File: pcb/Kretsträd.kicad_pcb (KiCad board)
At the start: 2 copper layers, 112.5 x 95.1 mm, 58 parts, among them J1 Conn_01x02_Female, J2 Conn_01x02_Female, J3 Conn_01x02_Female, SW1 SW_PUSH, SW10 SW_PUSH, SW11 SW_PUSH, SW12 SW_PUSH, SW13 SW_PUSH, SW14 SW_PUSH, SW15 SW_PUSH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

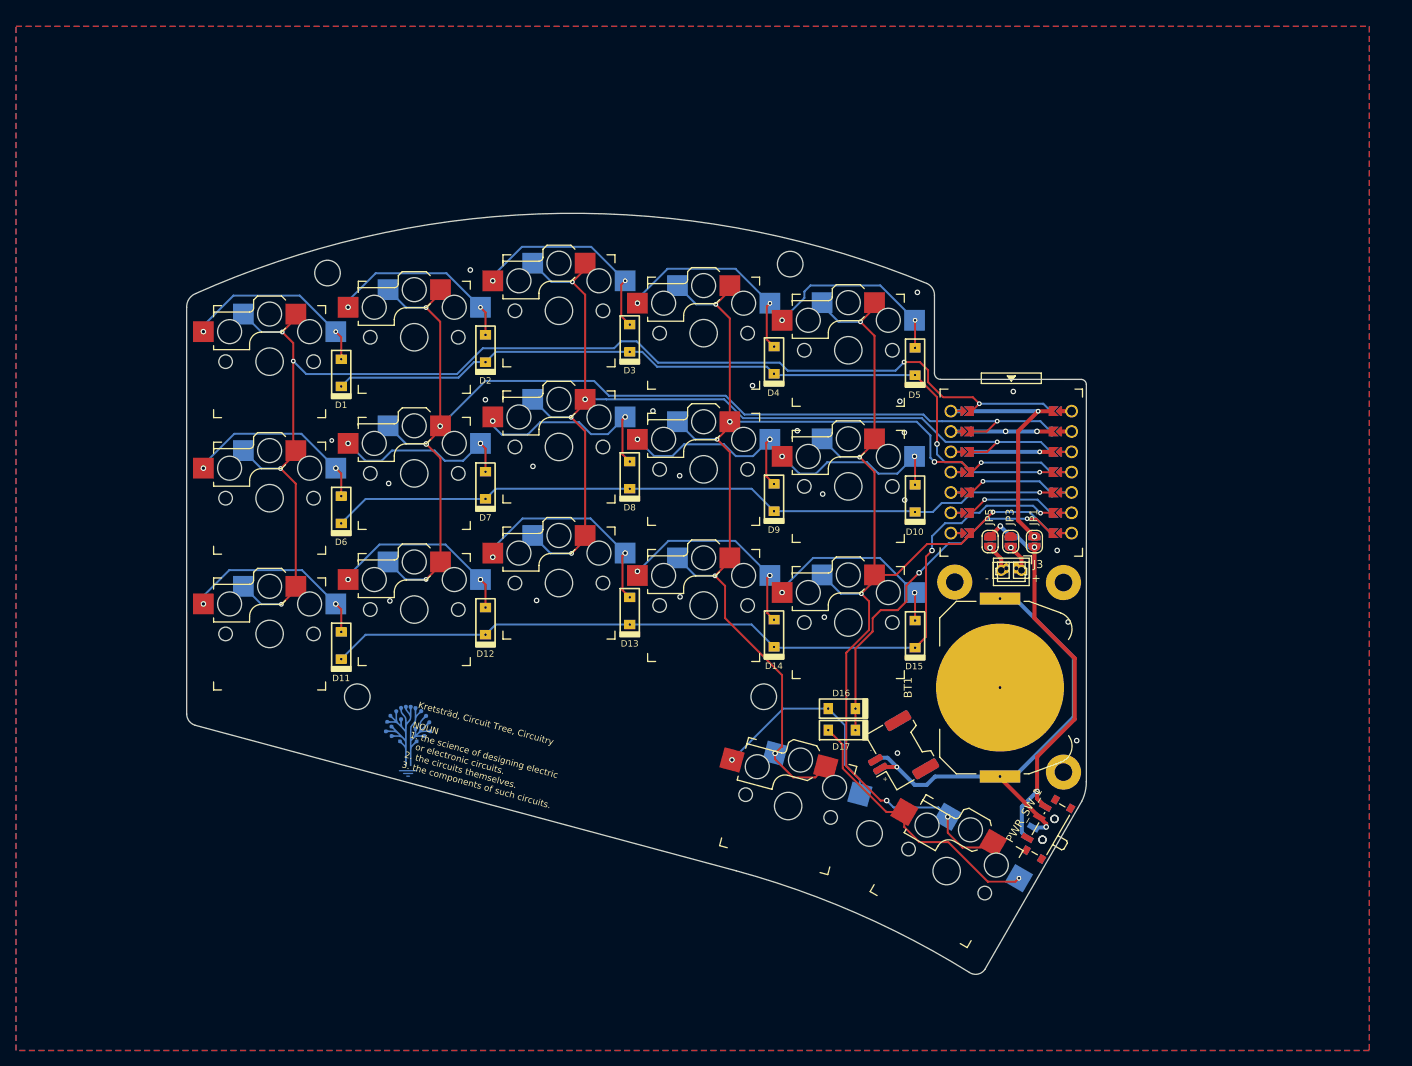
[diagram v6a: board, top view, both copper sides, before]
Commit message: 1. Updated switch footprint to increase solder pad size. 2. Squeezed MCU LIR2032 battery holder power switch section. 3. Re-routed a lot. 4. Reduced curvature on edge under thumb keys. 5. Removed power and ground pins selector jumper pads beneath MCU. 6. Other changes.
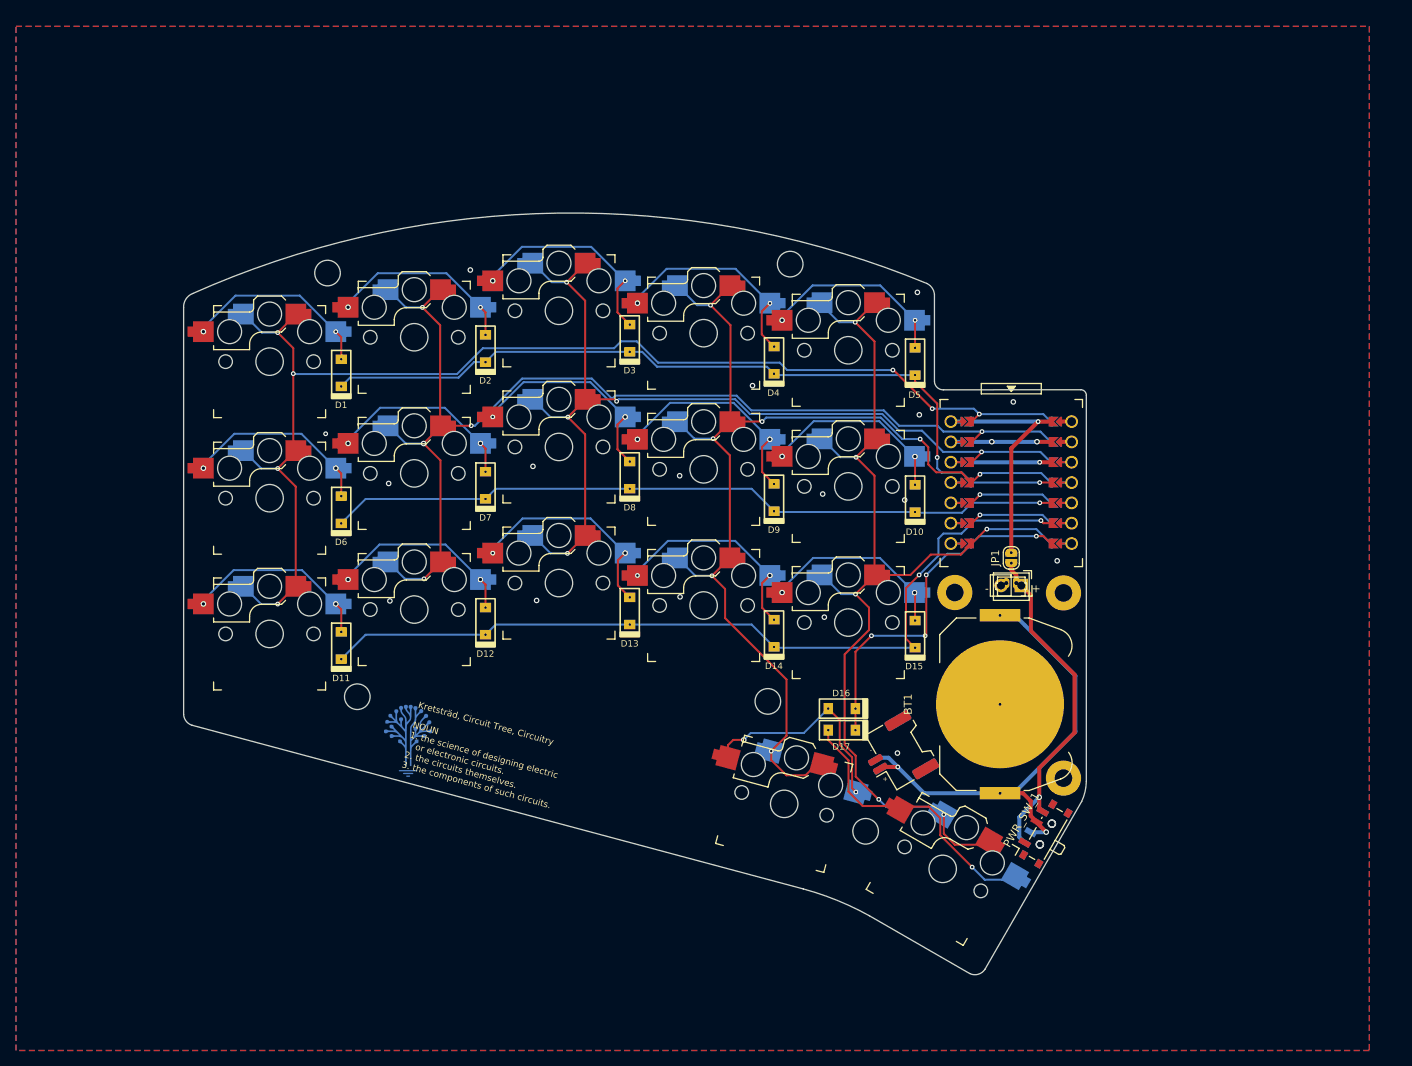
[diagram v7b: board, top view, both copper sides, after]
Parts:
- removed Hole_1, Hole_2: MountingHole_Pad, kbd:1pin_conn
- removed JP2: to_RAW, Jumper:SolderJumper-2_P1.3mm_Open_RoundedPad1.0x1.5mm
- removed JP3, JP4: Hole_1, Jumper:SolderJumper-2_P1.3mm_Open_RoundedPad1.0x1.5mm
- removed JP5, JP6: Hole_2, Jumper:SolderJumper-2_P1.3mm_Open_RoundedPad1.0x1.5mm
- added J4: Conn_01x02_Female, Connector_PinSocket_2.54mm:PinSocket_1x02_P2.54mm_Vertical, F.Cu at (183.4, 94.3)
- JP1: footprint Jumper:SolderJumper-2_P1.3mm_Open_RoundedPad1.0x1.5mm -> jw_custom_footprint:SolderJumper-2_P1.3mm_Open_RoundedPad1.0x1.5mm_dual_side
- moved JP1 3.54 mm to (182.2, 90.9)
- moved BT1 2.09 mm to (180.7, 109.2)
- moved J3 1.85 mm to (182.8, 94.0)
- moved U1 1.30 mm to (182.2, 81.3)
- moved TH_PCB_1 1.30 mm to (175.1, 95.2)
- moved TH_PCB_2 1.30 mm to (188.7, 95.3)
- moved TH5 0.77 mm to (151.7, 108.8)
- moved TH_PCB_3 0.75 mm to (188.7, 118.4)
- moved PWR_SW_1 0.68 mm to (186.2, 125.2)
- moved PWR_SW_2 0.68 mm to (186.2, 125.2)
- moved SW17 0.57 mm to (173.6, 129.7)
- moved TH4 0.57 mm to (163.9, 125.1)
- moved SW16 0.57 mm to (153.8, 121.6)
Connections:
- J3 pad 1: Hole_1 -> /PWR
- J3 pad 2: Hole_2 -> GND
- JP1 pad 1: Net-(JP1-Pad1) -> /PWR
- PWR_SW_1 pad 3: Net-(JP1-Pad1) -> /PWR
- PWR_SW_2 pad 3: Net-(JP1-Pad1) -> /PWR
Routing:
- net Net-(JP1-Pad1): track 51.0 -> 0.00 mm, vias 3 -> 0
- net /PWR: track 0.00 -> 42.7 mm, vias 0 -> 1
- net Hole_2: track 3.40 -> 0.00 mm, vias 1 -> 0
- net Hole_1: track 3.40 -> 0.00 mm, vias 1 -> 0
- net col0: track 159.0 -> 156.2 mm, vias 6 -> 7
- net col2: track 120.0 -> 117.7 mm
- net col4: track 127.4 -> 125.4 mm
- net col1: track 140.7 -> 138.9 mm
- net Net-(D9-Pad2): track 25.6 -> 27.2 mm
- net row0: track 100.7 -> 102.2 mm
- net Net-(D8-Pad2): track 25.8 -> 27.1 mm
- net Net-(D17-Pad2): track 34.7 -> 33.5 mm
- net Net-(D7-Pad2): track 23.2 -> 24.3 mm
- net Net-(D14-Pad2): track 26.0 -> 27.0 mm
- net Net-(D10-Pad2): track 23.1 -> 24.0 mm
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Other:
- board size 112.5 x 95.1 mm -> 112.8 x 95.2 mm
